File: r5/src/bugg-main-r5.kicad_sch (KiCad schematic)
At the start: 43 parts, among them T14 , T15 , T16 , T3 , T39 , T40 , U1 74LVC1G07DCK, U34 74LVC1G157GV

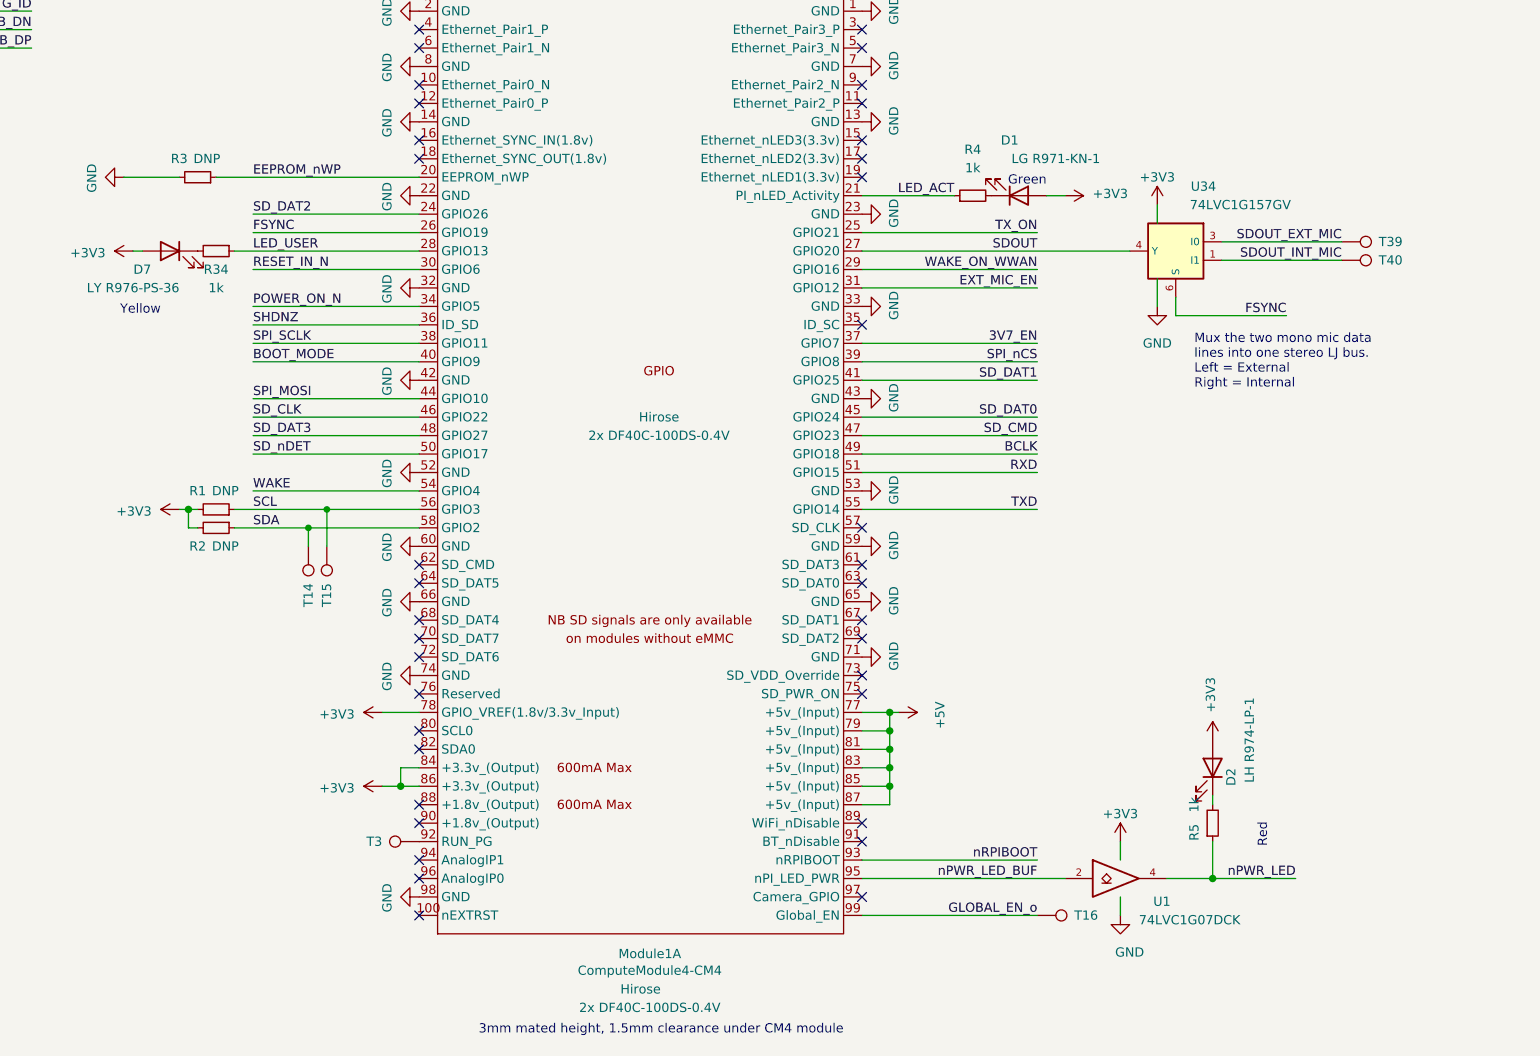
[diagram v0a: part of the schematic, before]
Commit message: Updates to +/-15V supply. Additional output capacitance. Change to smaller inductor packages. Add 0R links to permit isolation of output. Mods to compensation network. Set feedback resistors to datasheet values.
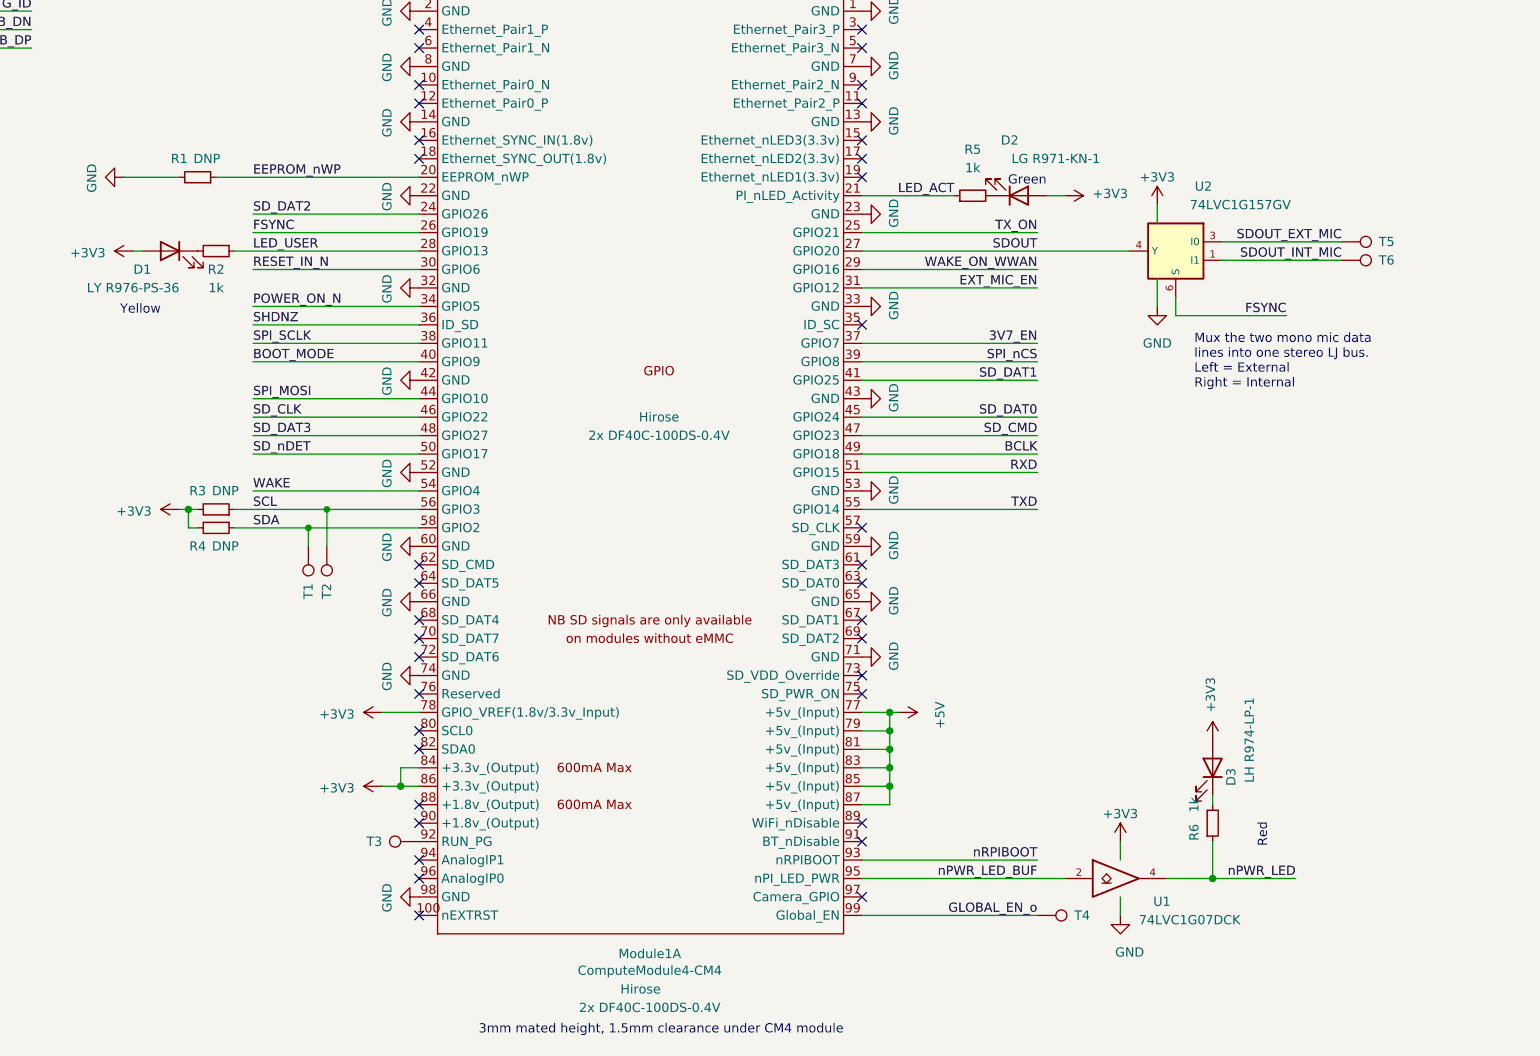
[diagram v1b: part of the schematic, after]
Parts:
- renumbered D7 to D1, D1 to D2, D2 to D3, R3 to R1, R34 to R2, R1 to R3, R2 to R4, R4 to R5, R5 to R6, T14 to T1, T15 to T2, T16 to T4, T39 to T5, T40 to T6, U34 to U2

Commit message: Fix broken component annotation by importing back from PCB and fixing duplicates.
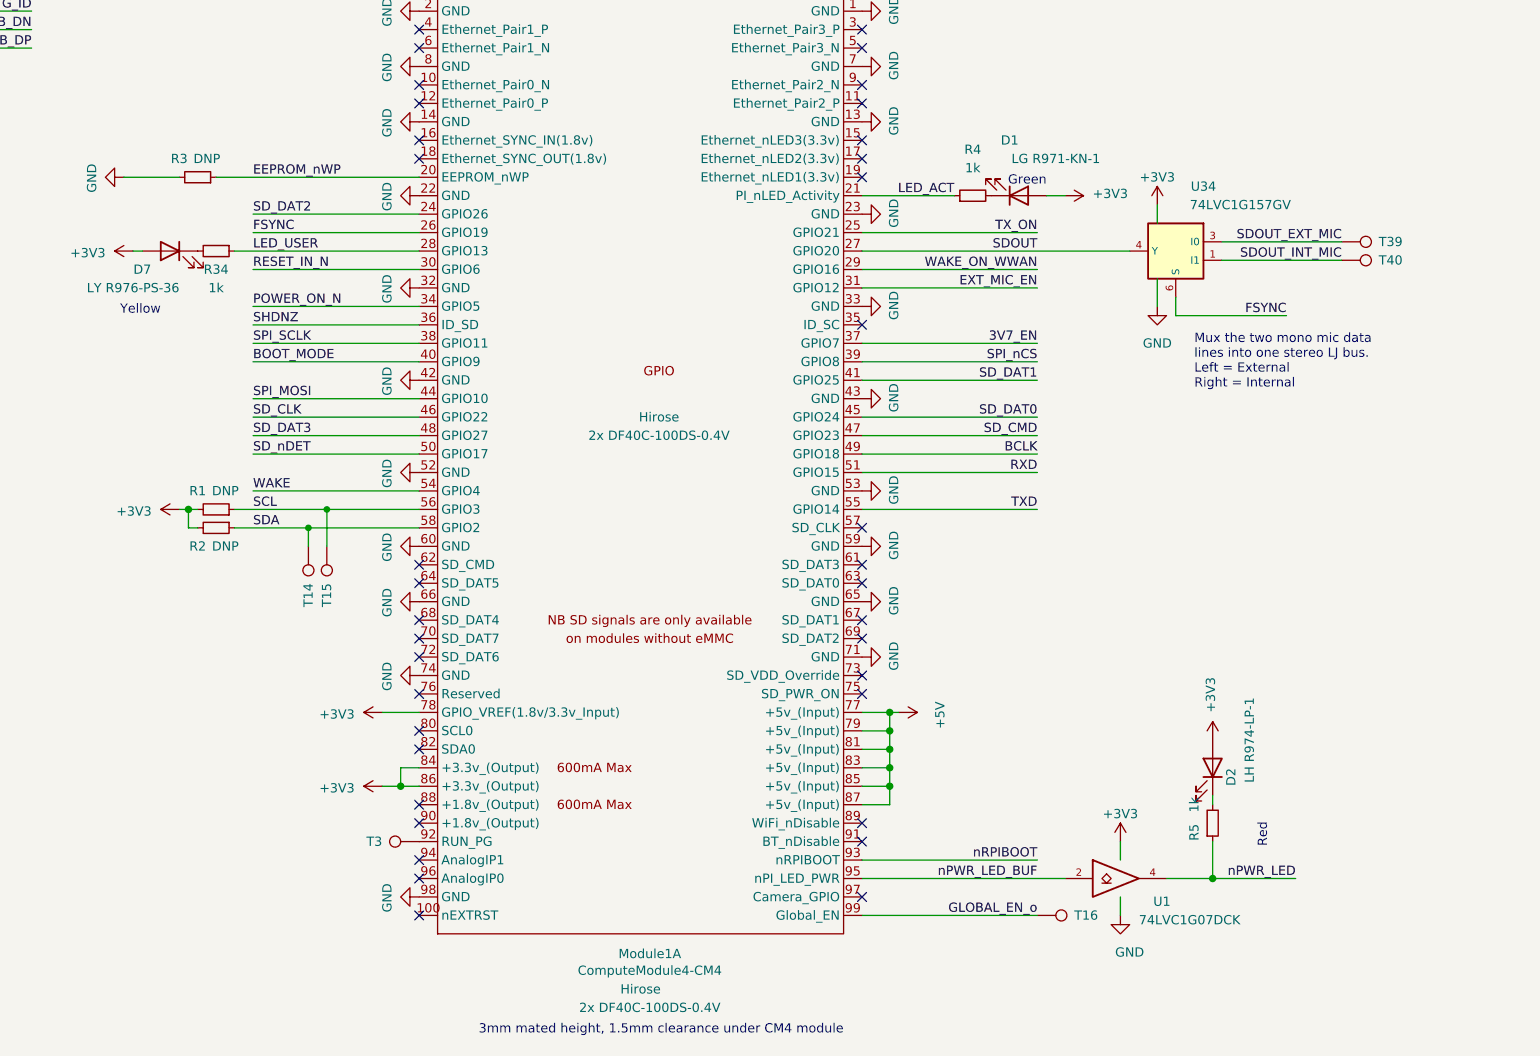
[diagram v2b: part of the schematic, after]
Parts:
- renumbered D2 to D1, D3 to D2, D1 to D7, R3 to R1, R4 to R2, R1 to R3, R2 to R34, R5 to R4, R6 to R5, T1 to T14, T2 to T15, T4 to T16, T5 to T39, T6 to T40, U2 to U34
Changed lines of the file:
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@@
   (symbol (lib_id "Device:R_Small") (at 151.13 106.68 270) (unit 1)
     (in_bom yes) (on_board yes) (dnp no)
-    (property "Reference" "R2" (at 151.13 109.22 90)
+    (property "Reference" "R34" (at 151.13 109.22 90)
       (effects (font (size 1.27 1.27)))
     )
@@
       (project "bugg-main-r5"
         (path "/e3eb514f-6ce4-4abe-ba20-f82f0015628f"
-          (reference "R2") (unit 1)
+          (reference "R34") (unit 1)
         )
       )
@@
   (symbol (lib_id "Device:R_Small") (at 255.27 99.06 90) (unit 1)
     (in_bom yes) (on_board yes) (dnp no)
-    (property "Reference" "R5" (at 255.27 92.71 90)
+    (property "Reference" "R4" (at 255.27 92.71 90)
       (effects (font (size 1.27 1.27)))
     )
@@
       (project "bugg-main-r5"
         (path "/e3eb514f-6ce4-4abe-ba20-f82f0015628f"
-          (reference "R5") (unit 1)
+          (reference "R4") (unit 1)
         )
       )
@@
   (symbol (lib_id "Device:LED") (at 144.78 106.68 0) (mirror y) (unit 1)
     (in_bom yes) (on_board yes) (dnp no)
-    (property "Reference" "D1" (at 140.97 109.22 0)
+    (property "Reference" "D7" (at 140.97 109.22 0)
       (effects (font (size 1.27 1.27)))
     )
@@
       (project "bugg-main-r5"
         (path "/e3eb514f-6ce4-4abe-ba20-f82f0015628f"
-          (reference "D1") (unit 1)
+          (reference "D7") (unit 1)
         )
       )
@@
   (symbol (lib_id "Connector:TestPoint") (at 306.07 105.41 270) (unit 1)
     (in_bom yes) (on_board yes) (dnp no)
-    (property "Reference" "T5" (at 311.15 105.41 90)
+    (property "Reference" "T39" (at 311.15 105.41 90)
       (effects (font (size 1.27 1.27)) (justify left))
     )
@@
       (project "bugg-main-r5"
         (path "/e3eb514f-6ce4-4abe-ba20-f82f0015628f"
-          (reference "T5") (unit 1)
+          (reference "T39") (unit 1)
         )
       )
@@
   (symbol (lib_id "Device:R_Small") (at 151.13 144.78 270) (unit 1)
     (in_bom yes) (on_board yes) (dnp no)
-    (property "Reference" "R4" (at 148.59 147.32 90)
+    (property "Reference" "R2" (at 148.59 147.32 90)
       (effects (font (size 1.27 1.27)))
     )
@@
       (project "bugg-main-r5"
         (path "/e3eb514f-6ce4-4abe-ba20-f82f0015628f"
-          (reference "R4") (unit 1)
+          (reference "R2") (unit 1)
         )
       )
@@
   (symbol (lib_id "Connector:TestPoint") (at 166.37 147.32 180) (unit 1)
     (in_bom yes) (on_board yes) (dnp no)
-    (property "Reference" "T2" (at 166.37 152.4 90)
+    (property "Reference" "T15" (at 166.37 152.4 90)
       (effects (font (size 1.27 1.27)) (justify left))
     )
@@
       (project "bugg-main-r5"
         (path "/e3eb514f-6ce4-4abe-ba20-f82f0015628f"
-          (reference "T2") (unit 1)
+          (reference "T15") (unit 1)
         )
       )
@@
   (symbol (lib_id "Device:R_Small") (at 151.13 142.24 270) (mirror x) (unit 1)
     (in_bom yes) (on_board yes) (dnp no)
-    (property "Reference" "R3" (at 148.59 139.7 90)
+    (property "Reference" "R1" (at 148.59 139.7 90)
       (effects (font (size 1.27 1.27)))
     )
@@
       (project "bugg-main-r5"
         (path "/e3eb514f-6ce4-4abe-ba20-f82f0015628f"
+          (reference "R1") (unit 1)
+        )
+      )
+    )
+  )
+  (symbol (lib_id "Device:R_Small") (at 148.59 96.52 270) (mirror x) (unit 1)
+    (in_bom yes) (on_board yes) (dnp no)
+    (property "Reference" "R3" (at 146.05 93.98 90)
+      (effects (font (size 1.27 1.27)))
+    )
+    (property "Value" "DNP" (at 149.86 93.98 90)
+      (effects (font (size 1.27 1.27)))
+    )
+    (property "Footprint" "Resistor_SMD:R_0402_1005Metric" (at 148.59 96.52 0)
+      (effects (font (size 1.27 1.27)) hide)
+    )
+    (property "Datasheet" "~" (at 148.59 96.52 0)
+      (effects (font (size 1.27 1.27)) hide)
+    )
+    (pin "1")
+    (pin "2")
+    (instances
+      (project "bugg-main-r5"
+        (path "/e3eb514f-6ce4-4abe-ba20-f82f0015628f"
           (reference "R3") (unit 1)
         )
@@
     )
   )
-  (symbol (lib_id "Device:R_Small") (at 148.59 96.52 270) (mirror x) (unit 1)
-    (in_bom yes) (on_board yes) (dnp no)
-    (property "Reference" "R1" (at 146.05 93.98 90)
-      (effects (font (size 1.27 1.27)))
-    )
-    (property "Value" "DNP" (at 149.86 93.98 90)
-      (effects (font (size 1.27 1.27)))
-    )
-    (property "Footprint" "Resistor_SMD:R_0402_1005Metric" (at 148.59 96.52 0)
-      (effects (font (size 1.27 1.27)) hide)
-    )
-    (property "Datasheet" "~" (at 148.59 96.52 0)
-      (effects (font (size 1.27 1.27)) hide)
-    )
-    (pin "1")
-    (pin "2")
-    (instances
-      (project "bugg-main-r5"
-        (path "/e3eb514f-6ce4-4abe-ba20-f82f0015628f"
-          (reference "R1") (unit 1)
-        )
-      )
-    )
-  )
   (symbol (lib_id "power:GND") (at 240.03 162.56 90) (unit 1)
     (in_bom yes) (on_board yes) (dnp no)
@@
   (symbol (lib_id "j_74xGxx:74LVC1G157") (at 283.21 106.68 0) (mirror y) (unit 1)
     (in_bom yes) (on_board yes) (dnp no)
-    (property "Reference" "U2" (at 287.02 97.79 0)
+    (property "Reference" "U34" (at 287.02 97.79 0)
       (effects (font (size 1.27 1.27)))
     )
@@
       (project "bugg-main-r5"
         (path "/e3eb514f-6ce4-4abe-ba20-f82f0015628f"
-          (reference "U2") (unit 1)
+          (reference "U34") (unit 1)
         )
       )
@@
         )
         (path "/e3eb514f-6ce4-4abe-ba20-f82f0015628f"
-          (reference "R9") (unit 1)
+          (reference "R77") (unit 1)
         )
       )
@@
   (symbol (lib_id "Device:LED") (at 288.29 177.8 270) (mirror x) (unit 1)
     (in_bom yes) (on_board yes) (dnp no)
-    (property "Reference" "D3" (at 290.83 179.07 0)
+    (property "Reference" "D2" (at 290.83 179.07 0)
       (effects (font (size 1.27 1.27)))
     )
@@
       (project "bugg-main-r5"
         (path "/e3eb514f-6ce4-4abe-ba20-f82f0015628f"
-          (reference "D3") (unit 1)
+          (reference "D2") (unit 1)
         )
       )
@@
         )
         (path "/e3eb514f-6ce4-4abe-ba20-f82f0015628f"
-          (reference "R7") (unit 1)
+          (reference "R75") (unit 1)
         )
       )
@@
   (symbol (lib_id "Connector:TestPoint") (at 264.16 198.12 270) (unit 1)
     (in_bom yes) (on_board yes) (dnp no)
-    (property "Reference" "T4" (at 269.24 198.12 90)
+    (property "Reference" "T16" (at 269.24 198.12 90)
       (effects (font (size 1.27 1.27)) (justify left))
     )
@@
       (project "bugg-main-r5"
         (path "/e3eb514f-6ce4-4abe-ba20-f82f0015628f"
-          (reference "T4") (unit 1)
+          (reference "T16") (unit 1)
         )
       )
@@
   (symbol (lib_id "Device:R_Small") (at 288.29 185.42 0) (mirror x) (unit 1)
     (in_bom yes) (on_board yes) (dnp no)
-    (property "Reference" "R6" (at 285.75 186.69 90)
+    (property "Reference" "R5" (at 285.75 186.69 90)
       (effects (font (size 1.27 1.27)))
     )
@@
       (project "bugg-main-r5"
         (path "/e3eb514f-6ce4-4abe-ba20-f82f0015628f"
-          (reference "R6") (unit 1)
+          (reference "R5") (unit 1)
         )
       )
@@
         )
         (path "/e3eb514f-6ce4-4abe-ba20-f82f0015628f"
-          (reference "R8") (unit 1)
+          (reference "R76") (unit 1)
         )
       )
@@
   (symbol (lib_id "Connector:TestPoint") (at 306.07 107.95 270) (unit 1)
     (in_bom yes) (on_board yes) (dnp no)
-    (property "Reference" "T6" (at 311.15 107.95 90)
+    (property "Reference" "T40" (at 311.15 107.95 90)
       (effects (font (size 1.27 1.27)) (justify left))
     )
@@
       (project "bugg-main-r5"
         (path "/e3eb514f-6ce4-4abe-ba20-f82f0015628f"
-          (reference "T6") (unit 1)
+          (reference "T40") (unit 1)
         )
       )
@@
   (symbol (lib_id "Device:LED") (at 261.62 99.06 0) (mirror x) (unit 1)
     (in_bom yes) (on_board yes) (dnp no)
-    (property "Reference" "D2" (at 260.35 91.44 0)
+    (property "Reference" "D1" (at 260.35 91.44 0)
       (effects (font (size 1.27 1.27)))
     )
@@
       (project "bugg-main-r5"
         (path "/e3eb514f-6ce4-4abe-ba20-f82f0015628f"
-          (reference "D2") (unit 1)
+          (reference "D1") (unit 1)
         )
       )
@@
   (symbol (lib_id "Connector:TestPoint") (at 163.83 147.32 180) (unit 1)
     (in_bom yes) (on_board yes) (dnp no)
-    (property "Reference" "T1" (at 163.83 152.4 90)
+    (property "Reference" "T14" (at 163.83 152.4 90)
       (effects (font (size 1.27 1.27)) (justify left))
     )
@@
       (project "bugg-main-r5"
         (path "/e3eb514f-6ce4-4abe-ba20-f82f0015628f"
-          (reference "T1") (unit 1)
-        )
-      )
+          (reference "T14") (unit 1)
+        )
+      )
